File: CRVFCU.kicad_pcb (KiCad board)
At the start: 4 copper layers, 1 part, among them U2 STM32H747IITx

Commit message: completed grouping in pcb, prep for route
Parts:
- added 3V3_PWR1: LED, LED_SMD:LED_0603_1608Metric, F.Cu at (95.3, 149.5)
- added 5V_PWR1: LED, LED_SMD:LED_0603_1608Metric, F.Cu at (96.5, 153.8)
- added ARM1: TERM2.54_01x04, TerminalBlock_TE-Connectivity:TerminalBlock_TE_282834-4_1x04_P2.54mm_Horizontal, F.Cu at (44.0, 102.6)
- added BATT1: AMASS_XT30, Connector_AMASS:AMASS_XT30U-F_1x02_P5.0mm_Vertical, F.Cu at (70.0, 116.0)
- added BZ2: Buzzer, Buzzer_Beeper:Buzzer_CUI_CPT-9019S-SMT, F.Cu at (117.7, 84.6)
- added C1: 100uF, Capacitor_THT:CP_Radial_D8.0mm_P5.00mm, F.Cu at (74.8, 110.4)
- added C10: 1uF, Capacitor_SMD:C_0402_1005Metric, B.Cu at (230.0, 30.9)
- added C11: 4.7uF, Capacitor_SMD:C_0402_1005Metric, B.Cu at (250.9, 49.1)
- added C12: 220pF, Capacitor_SMD:C_0402_1005Metric, B.Cu at (249.6, 50.4)
- added C13: 2.2uF, Capacitor_SMD:C_0402_1005Metric, B.Cu at (239.6, 52.3)
- added C14: 2.2uF, Capacitor_SMD:C_0402_1005Metric, B.Cu at (225.2, 37.7)
- added C15: 2.2uF, Capacitor_SMD:C_0402_1005Metric, B.Cu at (233.9, 26.9)
- added C16: 100nF, Capacitor_SMD:C_0402_1005Metric, B.Cu at (234.6, 27.7)
- added C17: 10uF, Capacitor_SMD:C_0402_1005Metric, B.Cu at (256.8, 39.2)
- added C18: 100nF, Capacitor_SMD:C_0402_1005Metric, B.Cu at (257.6, 40.0)
- added C19: 100nF, Capacitor_SMD:C_0402_1005Metric, B.Cu at (247.8, 47.6)
- added C2: 10uF, Capacitor_SMD:C_0402_1005Metric, F.Cu at (68.5, 108.7)
- added C20: 100nF, Capacitor_SMD:C_0402_1005Metric, B.Cu at (232.4, 28.3)
- added C21: 100nF, Capacitor_SMD:C_0402_1005Metric, B.Cu at (237.0, 23.6)
- added C22: 100nF, Capacitor_SMD:C_0402_1005Metric, B.Cu at (239.6, 21.1)
- added C23: 100nF, Capacitor_SMD:C_0402_1005Metric, B.Cu at (245.5, 21.2)
- added C24: 100nF, Capacitor_SMD:C_0402_1005Metric, B.Cu at (246.9, 22.6)
- added C25: 100nF, Capacitor_SMD:C_0402_1005Metric, B.Cu at (250.2, 25.9)
- added C26: 100nF, Capacitor_SMD:C_0402_1005Metric, B.Cu at (252.4, 28.1)
- added C27: 100nF, Capacitor_SMD:C_0402_1005Metric, B.Cu at (258.5, 34.2)
- added C28: 100nF, Capacitor_SMD:C_0402_1005Metric, B.Cu at (260.2, 37.3)
- added C29: 100nF, Capacitor_SMD:C_0402_1005Metric, B.Cu at (252.3, 45.5)
- added C30: 100nF, Capacitor_SMD:C_0402_1005Metric, B.Cu at (246.1, 51.7)
- added C31: 100nF, Capacitor_SMD:C_0402_1005Metric, B.Cu at (246.4, 48.9)
- added C32: 100nF, Capacitor_SMD:C_0402_1005Metric, B.Cu at (227.4, 33.0)
- added C33: 100nF, Capacitor_SMD:C_0402_1005Metric, B.Cu at (232.1, 45.0)
- added C34: 100nF, Capacitor_SMD:C_0402_1005Metric, B.Cu at (241.2, 53.9)
- added C35: 100nF, Capacitor_SMD:C_0402_1005Metric, B.Cu at (225.4, 40.1)
- added C36: 4.7uF, Capacitor_SMD:C_0402_1005Metric, B.Cu at (226.6, 39.1)
- added C37: 1.5pF, Capacitor_SMD:C_0402_1005Metric, F.Cu at (251.3, 52.5)
- added C38: 1.5pF, Capacitor_SMD:C_0402_1005Metric, F.Cu at (249.9, 53.9)
- added C39: 100nF, Capacitor_SMD:C_0402_1005Metric, B.Cu at (234.9, 47.8)
- added C4: 10uF, Capacitor_SMD:C_0402_1005Metric, F.Cu at (52.4, 94.1)
- added C41: 100nF, Capacitor_SMD:C_0402_1005Metric, F.Cu at (257.0, 42.3)
- added C42: 220nF, Capacitor_SMD:C_0402_1005Metric, B.Cu at (137.0, 164.8)
- added C43: 10uF, Capacitor_SMD:C_0402_1005Metric, B.Cu at (139.0, 163.8)
- added C44: 100nF, Capacitor_SMD:C_0402_1005Metric, B.Cu at (138.9, 162.6)
- added C45: 100nF, Capacitor_SMD:C_0402_1005Metric, B.Cu at (139.0, 164.8)
- added C46: 100nF, Capacitor_SMD:C_0402_1005Metric, B.Cu at (148.1, 162.3)
- added C47: 100nF, Capacitor_SMD:C_0402_1005Metric, B.Cu at (160.1, 164.3)
- added C48: 100nF, Capacitor_SMD:C_0402_1005Metric, B.Cu at (158.2, 164.3)
- added C49: 10nF, Capacitor_SMD:C_0402_1005Metric, F.Cu at (166.3, 163.8)
- added C5: 10uF, Capacitor_SMD:C_0402_1005Metric, F.Cu at (62.3, 89.1)
- added C50: 100nF, Capacitor_SMD:C_0402_1005Metric, F.Cu at (260.5, 46.3)
- added C51: 100nF, Capacitor_SMD:C_0402_1005Metric, B.Cu at (252.3, 41.3)
- added C6: 10uF, Capacitor_SMD:C_0402_1005Metric, F.Cu at (62.3, 91.5)
- added C7: 10uF, Capacitor_SMD:C_0402_1005Metric, F.Cu at (52.3, 104.7)
- added C8: 10uF, Capacitor_SMD:C_0402_1005Metric, F.Cu at (62.3, 100.2)
- added C9: 10uF, Capacitor_SMD:C_0402_1005Metric, F.Cu at (62.3, 102.5)
- added D1: MBR0540, Diode_SMD:D_SOD-123, F.Cu at (59.4, 95.5)
- added D2: MBR0540, Diode_SMD:D_SOD-123, F.Cu at (59.3, 106.5)
- added H1: MountingHole_Pad, MountingHole:MountingHole_3.2mm_M3_Pad, F.Cu at (44.0, 116.0)
- added H2: MountingHole_Pad, MountingHole:MountingHole_3.2mm_M3_Pad, F.Cu at (-23.0, 91.0)
- added H3: MountingHole_Pad, MountingHole:MountingHole_3.2mm_M3_Pad, F.Cu at (-23.0, 99.0)
- added H4: MountingHole_Pad, MountingHole:MountingHole_3.2mm_M3_Pad, F.Cu at (86.0, 116.0)
- added J1: TagConnect_TC2030, Connector:Tag-Connect_TC2030-IDC-NL_2x03_P1.27mm_Vertical, F.Cu at (213.4, 77.3)
- added J3: USB_C_Receptacle_USB2.0_16P, Connector_USB:USB_C_Receptacle_GCT_USB4105-xx-A_16P_TopMnt_Horizontal, F.Cu at (131.9, 65.9)
- added J4: Micro_SD_Card_Det2, Connector_Card:microSD_HC_Hirose_DM3AT-SF-PEJM5, B.Cu at (49.2, 28.4)
- added L1: 1608KF-601T03, Inductor_SMD:L_0603_1608Metric, B.Cu at (256.8, 37.4)
- added L2: FBMJ1608HM180NTR, Inductor_SMD:L_0603_1608Metric, B.Cu at (250.0, 47.2)
- added L3: 2.2uH, Inductor_SMD:L_0603_1608Metric, B.Cu at (247.8, 49.4)
- added LED1: LED, LED_SMD:LED_0603_1608Metric, F.Cu at (110.1, 157.0)
- added NEOPIX1: WS2812B-2020, LED_SMD:LED_WS2812B-2020_PLCC4_2.0x2.0mm, F.Cu at (149.3, 127.7)
- added PWM0: JST_XH_B3B-XH-AM, Connector_PinHeader_2.54mm:PinHeader_1x03_P2.54mm_Vertical, F.Cu at (47.1, 88.0)
- added PWM1: JST_XH_B3B-XH-AM, Connector_PinHeader_2.54mm:PinHeader_1x03_P2.54mm_Vertical, F.Cu at (47.1, 91.6)
- added PWM2: JST_XH_B3B-XH-AM, Connector_PinHeader_2.54mm:PinHeader_1x03_P2.54mm_Vertical, F.Cu at (47.1, 95.2)
- added PWM3: JST_XH_B3B-XH-AM, Connector_PinHeader_2.54mm:PinHeader_1x03_P2.54mm_Vertical, F.Cu at (47.1, 98.8)
- added PWM4: JST_XH_B3B-XH-AM, Connector_PinHeader_2.54mm:PinHeader_1x03_P2.54mm_Vertical, F.Cu at (50.0, 112.9)
- added PWM5: JST_XH_B3B-XH-AM, Connector_PinHeader_2.54mm:PinHeader_1x03_P2.54mm_Vertical, F.Cu at (53.6, 112.9)
- added PWM6: JST_XH_B3B-XH-AM, Connector_PinHeader_2.54mm:PinHeader_1x03_P2.54mm_Vertical, F.Cu at (57.2, 112.9)
- added PWM7: JST_XH_B3B-XH-AM, Connector_PinHeader_2.54mm:PinHeader_1x03_P2.54mm_Vertical, F.Cu at (60.8, 112.9)
- added PYRO_TERM1: TERM2.54_01x10, TerminalBlock_TE-Connectivity:TerminalBlock_TE_1-282834-0_1x10_P2.54mm_Horizontal, F.Cu at (86.0, 109.9)
- added Q3: DMG2301L, Package_TO_SOT_SMD:SOT-23, F.Cu at (54.9, 96.0)
- added Q4: BC818, Package_TO_SOT_SMD:SOT-23, F.Cu at (119.3, 94.5)
- added Q5: DMG2301L, Package_TO_SOT_SMD:SOT-23, F.Cu at (250.2, 71.7)
- added Q6: DMG2301L, Package_TO_SOT_SMD:SOT-23, F.Cu at (54.9, 107.1)
- added R1: 10k, Resistor_SMD:R_Array_Convex_4x0402, F.Cu at (215.0, 74.1)
- added R10: 10k, Resistor_SMD:R_0402_1005Metric, B.Cu at (62.3, 108.2)
- added R11: 3.3k, Resistor_SMD:R_0402_1005Metric, B.Cu at (77.1, 100.5)
- added R12: 1k, Resistor_SMD:R_0402_1005Metric, B.Cu at (77.1, 99.5)
- added R13: 5.1k, Resistor_SMD:R_0402_1005Metric, F.Cu at (137.7, 63.9)
- added R14: 180k, Resistor_SMD:R_0402_1005Metric, B.Cu at (81.1, 98.6)
- added R15: 10k, Resistor_SMD:R_Array_Convex_2x0402, F.Cu at (147.6, 135.4)
- added R16: 56k, Resistor_SMD:R_0402_1005Metric, B.Cu at (79.1, 98.6)
- added R17: 5.1k, Resistor_SMD:R_0402_1005Metric, F.Cu at (137.7, 68.4)
- added R18: 47R, Resistor_SMD:R_0402_1005Metric, F.Cu at (161.2, 163.4)
- added R19: 3.3k, Resistor_SMD:R_0402_1005Metric, B.Cu at (77.1, 102.5)
- added R2: 10k, Resistor_SMD:R_0402_1005Metric, F.Cu at (58.0, 97.2)
- added R20: 10k, Resistor_SMD:R_0402_1005Metric, B.Cu at (158.2, 163.3)
- added R21: 10k, Resistor_SMD:R_0402_1005Metric, B.Cu at (148.1, 164.7)
- added R22: 10k, Resistor_SMD:R_0402_1005Metric, B.Cu at (137.0, 163.8)
- added R23: 10k, Resistor_SMD:R_0402_1005Metric, B.Cu at (248.5, 45.2)
- added R24: 10k, Resistor_SMD:R_0402_1005Metric, B.Cu at (59.3, 34.2)
- added R25: 1k, Resistor_SMD:R_0402_1005Metric, B.Cu at (77.1, 101.5)
- added R26: 180k, Resistor_SMD:R_0402_1005Metric, B.Cu at (81.1, 103.4)
- added R27: 56k, Resistor_SMD:R_0402_1005Metric, B.Cu at (79.1, 103.4)
- added R28: 3.3k, Resistor_SMD:R_0402_1005Metric, B.Cu at (77.1, 90.1)
- added R29: 1k, Resistor_SMD:R_0402_1005Metric, B.Cu at (77.1, 89.1)
- added R30: 180k, Resistor_SMD:R_0402_1005Metric, B.Cu at (81.1, 88.4)
- added R31: 56k, Resistor_SMD:R_0402_1005Metric, B.Cu at (79.1, 88.4)
- added R32: 3.3k, Resistor_SMD:R_0402_1005Metric, B.Cu at (77.1, 92.1)
- added R33: 1k, Resistor_SMD:R_0402_1005Metric, B.Cu at (77.1, 91.1)
- added R34: 180k, Resistor_SMD:R_0402_1005Metric, B.Cu at (81.1, 93.2)
- added R35: 56k, Resistor_SMD:R_0402_1005Metric, B.Cu at (79.1, 93.2)
- added R36: 220R, Resistor_SMD:R_0402_1005Metric, B.Cu at (96.5, 153.8)
- added R37: 220R, Resistor_SMD:R_0402_1005Metric, B.Cu at (95.2, 149.5)
- added R38: 47R, Resistor_SMD:R_Array_Convex_4x0402, B.Cu at (50.1, 94.0)
- added R39: 47R, Resistor_SMD:R_Array_Convex_4x0402, B.Cu at (55.5, 109.9)
- added R4: 47R1%, Resistor_SMD:R_0402_1005Metric, B.Cu at (258.6, 41.1)
- added R40: 10k, Resistor_SMD:R_0402_1005Metric, F.Cu at (125.6, 93.3)
- added R41: 2.2k, Resistor_SMD:R_0402_1005Metric, F.Cu at (125.1, 90.9)
- added R42: 220R, Resistor_SMD:R_0402_1005Metric, F.Cu at (109.8, 159.8)
- added R43: 10k, Resistor_SMD:R_0402_1005Metric, B.Cu at (50.4, 104.0)
- added R44: 47R, Resistor_SMD:R_0402_1005Metric, B.Cu at (50.4, 105.1)
- added R45: 10k, Resistor_SMD:R_0402_1005Metric, F.Cu at (247.6, 71.7)
- added R5: 10k, Resistor_SMD:R_0402_1005Metric, B.Cu at (239.2, 54.0)
- added R6: 10k, Resistor_SMD:R_0402_1005Metric, B.Cu at (237.4, 49.9)
- added R7: 10k, Resistor_SMD:R_0402_1005Metric, F.Cu at (166.3, 162.0)
- added R8: 51, Resistor_SMD:R_0402_1005Metric, F.Cu at (256.3, 43.6)
- added R9: 10k, Resistor_SMD:R_0402_1005Metric, F.Cu at (261.8, 45.0)
- added RADIO_5VPWR_3V3IO1: JST_GH_SM06B, Connector_JST:JST_GH_SM06B-GHS-TB_1x06-1MP_P1.25mm_Horizontal, F.Cu at (229.4, 76.0)
- added STEMMA_QT1: JST_SH_SM04B, Connector_JST:JST_SH_SM04B-SRSS-TB_1x04-1MP_P1.00mm_Horizontal, F.Cu at (120.7, 139.1)
- added SW1: SW_Omron_B3FS, Button_Switch_SMD:SW_SPST_FSMSM, F.Cu at (263.4, 36.3)
- added SW2: SW_Nidec_CAS-120A1, Button_Switch_SMD:Nidec_Copal_CAS-120A, F.Cu at (235.0, 52.4)
- added U1: MS5611-01BA, Package_LGA:LGA-8_3x5mm_P1.25mm, F.Cu at (149.1, 163.5)
- added U10: W25Q128JVS, Package_SO:SOIC-8_5.3x5.3mm_P1.27mm, B.Cu at (247.5, 41.3)
- added U11: CM1624, Package_DFN_QFN:OnSemi_UDFN-16-1EP_1.35x3.3mm_P0.4mm_EP0.4x2.8mm, B.Cu at (59.3, 29.0)
- added U12: ~, Package_TO_SOT_SMD:SOT-353_SC-70-5, F.Cu at (212.1, 73.6)
- added U13: USBLC6-2SC6, Package_TO_SOT_SMD:SOT-23-6, F.Cu at (121.6, 132.5)
- added U14: USBLC6-2SC6, Package_TO_SOT_SMD:SOT-23-6, F.Cu at (138.8, 66.2)
- added U15: MAX17049, Package_DFN_QFN:TDFN-8-1EP_2x2mm_P0.5mm_EP0.8x1.2mm, F.Cu at (144.6, 136.0)
- added U16: SI7232DN-T1, FCU2025Lib:SQJ500AEP-T1_GE3_VIS, B.Cu at (79.9, 90.8)
- added U17: SN74LV1T34DCK, Package_TO_SOT_SMD:SOT-353_SC-70-5, B.Cu at (149.3, 127.6)
- added U3: LIS2MDL, Package_LGA:LGA-12_2x2mm_P0.5mm, F.Cu at (138.3, 163.6)
- added U4: ICM-45686, Package_LGA:LGA-14_3x2.5mm_P0.5mm_LayoutBorder3x4y, F.Cu at (158.8, 163.3)
- added U5: FXMA108, Package_DFN_QFN:WQFN-20-1EP_2.5x4.5mm_P0.5mm_EP1x2.9mm, B.Cu at (59.1, 105.9)
- added U6: AP1117-50, Package_TO_SOT_SMD:SOT-223-3_TabPin2, F.Cu at (57.3, 90.6)
- added U7: AP1117-33, Package_TO_SOT_SMD:SOT-223-3_TabPin2, F.Cu at (57.4, 101.6)
- added U8: SI7232DN-T1, FCU2025Lib:SQJ500AEP-T1_GE3_VIS, B.Cu at (79.9, 101.0)
- added U9: USBLC6-4SC6, Package_TO_SOT_SMD:SOT-23-6, F.Cu at (229.0, 69.9)
- added VIDEO1: JST_GH_SM02B, Connector_JST:JST_GH_SM02B-GHS-TB_1x02-1MP_P1.25mm_Horizontal, F.Cu at (249.9, 77.9)
- added Y1: 32.768khz, Crystal:Crystal_SMD_3215-2Pin_3.2x1.5mm, F.Cu at (249.0, 51.8)
- added Y3: 32.768khz, Oscillator:Oscillator_SMD_Abracon_ASE-4Pin_3.2x2.5mm, F.Cu at (163.7, 163.1)
- added Y4: 25MHZ, Oscillator:Oscillator_SMD_Abracon_ASE-4Pin_3.2x2.5mm, F.Cu at (259.5, 43.6)
- moved U2 206.3 mm to (242.4, 36.8), turned to 135 degrees
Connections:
- U2 pad 1: unconnected-(U2-PE2-Pad1) -> /BUZZ
- U2 pad 10: unconnected-(U2-PC14-Pad10) -> /PC14
- U2 pad 101: unconnected-(U2-VCAPDSI-Pad101) -> /VDD12DSI
- U2 pad 102: +1V2 -> /VDD12DSI
- U2 pad 108: +1V2 -> /VDD12DSI
- U2 pad 11: unconnected-(U2-PC15-Pad11) -> /PC15
- U2 pad 116: unconnected-(U2-PG6-Pad116) -> /FLASH_CS
- U2 pad 120: unconnected-(U2-VDD50_USB-Pad120) -> +3V3
- U2 pad 124: unconnected-(U2-PC8-Pad124) -> /SD_DAT0
- U2 pad 125: unconnected-(U2-PC9-Pad125) -> /SD_DAT1
- U2 pad 130: unconnected-(U2-PA11-Pad130) -> /USB_D-
- U2 pad 131: unconnected-(U2-PA12-Pad131) -> /USB_D+
- U2 pad 132: unconnected-(U2-PA13-Pad132) -> /SWDIO
- U2 pad 133: unconnected-(U2-VCAP-Pad133) -> Net-(C13-Pad1)
- U2 pad 138: unconnected-(U2-PA14-Pad138) -> /SWCLK
- U2 pad 140: unconnected-(U2-PC10-Pad140) -> /SD_DAT2
- U2 pad 141: unconnected-(U2-PC11-Pad141) -> /SD_DAT3
- U2 pad 142: unconnected-(U2-PC12-Pad142) -> /SD_CLK
- U2 pad 143: unconnected-(U2-PD0-Pad143) -> /RAD_RX
- U2 pad 144: unconnected-(U2-PD1-Pad144) -> /RAD_TX
- U2 pad 145: unconnected-(U2-PD2-Pad145) -> /SD_CMD
- U2 pad 146: unconnected-(U2-PD3-Pad146) -> /SD_DET
- U2 pad 147: unconnected-(U2-PD4-Pad147) -> /SRV_OE
- U2 pad 148: unconnected-(U2-PD5-Pad148) -> /SRVI_0
- U2 pad 149: unconnected-(U2-PD6-Pad149) -> /SRVI_1
- U2 pad 15: unconnected-(U2-VLXSMPS-Pad15) -> /VLXSMPS
- U2 pad 150: unconnected-(U2-PD7-Pad150) -> /SRVI_2
- U2 pad 153: unconnected-(U2-PG9-Pad153) -> /SRVI_3
- U2 pad 154: unconnected-(U2-PG10-Pad154) -> /SRVI_4
- U2 pad 155: unconnected-(U2-PG11-Pad155) -> /SRVI_5
- U2 pad 156: unconnected-(U2-PG12-Pad156) -> /SRVI_6
- U2 pad 157: unconnected-(U2-PG13-Pad157) -> /SRVI_7
- U2 pad 16: +3V3 -> /VDDSMPS
- U2 pad 162: unconnected-(U2-PB3-Pad162) -> /SWO
- U2 pad 167: unconnected-(U2-BOOT0-Pad167) -> Net-(U2-BOOT0)
- U2 pad 17: unconnected-(U2-VFBSMPS-Pad17) -> +3V3
- U2 pad 172: unconnected-(U2-VCAP-Pad172) -> Net-(C13-Pad1)
- U2 pad 174: unconnected-(U2-PDR_ON-Pad174) -> Net-(U2-PDR_ON)
- U2 pad 18: unconnected-(U2-PF0-Pad18) -> /VIDEO
- U2 pad 19: unconnected-(U2-PF1-Pad19) -> /ARM
- U2 pad 20: unconnected-(U2-PF2-Pad20) -> /LED
- U2 pad 21: unconnected-(U2-PF3-Pad21) -> /NEOPIX
- U2 pad 26: unconnected-(U2-PF6-Pad26) -> /QSPI_IO3
- U2 pad 27: unconnected-(U2-PF7-Pad27) -> /QSPI_IO2
- U2 pad 28: unconnected-(U2-PF8-Pad28) -> /QSPI_IO0
- U2 pad 29: unconnected-(U2-PF9-Pad29) -> /QSPI_IO1
- U2 pad 30: unconnected-(U2-PF10-Pad30) -> /QSPI_CLK
- U2 pad 31: unconnected-(U2-PH0-Pad31) -> /OSC0
- U2 pad 33: unconnected-(U2-NRST-Pad33) -> /RESET
- U2 pad 39: unconnected-(U2-VREF+-Pad39) -> Net-(U2-VREF+)
- U2 pad 40: +3V3 -> /VDDA
- U2 pad 46: unconnected-(U2-PA3-Pad46) -> /IMU_INT
- U2 pad 50: unconnected-(U2-PA5-Pad50) -> /SCK
- U2 pad 51: unconnected-(U2-PA6-Pad51) -> /MISO
- U2 pad 52: unconnected-(U2-PA7-Pad52) -> /MOSI
- U2 pad 53: unconnected-(U2-PC4-Pad53) -> /ALT_CS
- U2 pad 54: unconnected-(U2-PC5-Pad54) -> /IMU_CS
- U2 pad 55: unconnected-(U2-PB0-Pad55) -> /MAG_CS
- U2 pad 67: unconnected-(U2-PE7-Pad67) -> /PYR0
- U2 pad 68: unconnected-(U2-PE8-Pad68) -> /PYC0
- U2 pad 69: unconnected-(U2-PE9-Pad69) -> /PYR1
- U2 pad 72: unconnected-(U2-PE10-Pad72) -> /PYC1
- U2 pad 73: unconnected-(U2-PE11-Pad73) -> /PYR2
- U2 pad 74: unconnected-(U2-PE12-Pad74) -> /PYC2
- U2 pad 75: unconnected-(U2-PE13-Pad75) -> /PYR3
- U2 pad 76: unconnected-(U2-PE14-Pad76) -> /PYC3
- U2 pad 78: unconnected-(U2-PB10-Pad78) -> /SCL
- U2 pad 79: unconnected-(U2-PB11-Pad79) -> /SDA
- U2 pad 80: unconnected-(U2-VCAP-Pad80) -> Net-(C13-Pad1)
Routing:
- net +3V3: track 0.00 -> 76.1 mm, vias 0 -> 38
- net unconnected-(J4-SHIELD-Pad11): track 0.00 -> 42.3 mm
- net GND: track 0.00 -> 41.9 mm, vias 0 -> 28
- net VBUS: track 0.00 -> 41.0 mm
- net /FLASH_CS: track 0.00 -> 25.7 mm, vias 0 -> 1
- net +8V4: track 0.00 -> 23.7 mm
- net Net-(J4-DET_A): track 0.00 -> 23.6 mm
- net Net-(U5-B3): track 0.00 -> 14.9 mm
- net Net-(U5-B2): track 0.00 -> 14.8 mm
- net Net-(U5-B1): track 0.00 -> 14.7 mm
- net Net-(U5-B0): track 0.00 -> 14.7 mm
- net +5V: track 0.00 -> 13.8 mm, vias 0 -> 2
- net /SWDIO: track 0.00 -> 10.6 mm
- net /QSPI_IO2: track 0.00 -> 10.0 mm, vias 0 -> 1
- net /QSPI_IO1: track 0.00 -> 9.42 mm, vias 0 -> 1
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- added copper zone on F.Cu, net +3V3
- added copper zone on In2.Cu, net +3V3
- added copper zone on F.Cu, net +5V
- added copper zone on B.Cu, net +8V4
- added copper zone on B.Cu, net /PYO0
- added copper zone on B.Cu, net /PYO1
- added copper zone on B.Cu, net /PYO2
- added copper zone on B.Cu, net /PYO3
- added copper zone on F.Cu, net /VPYRO
- added copper zone on B.Cu, net GND
- added copper zone on F.Cu, net GND
- added copper zone on In1.Cu, net GND
- added copper zone on F.Cu, net Net-(D2-K)
- added copper zone on F.Cu, net Net-(Q3-S)
- added copper zone on F.Cu, net VBAT
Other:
- board outline added: 50 x 100 mm

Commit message: completed 50x100 routing, attempting 40mm
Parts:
- added C40: 100nF, Capacitor_SMD:C_0402_1005Metric, B.Cu at (44.5, 64.7)
- R42: moved to B.Cu
- moved VIDEO1 206.9 mm to (43.2, 69.4), turned to -90 degrees
- moved Q5 200.8 mm to (49.4, 69.7), turned to -90 degrees
- moved C23 198.3 mm to (49.4, 51.0), turned to 45 degrees
- moved R45 198.3 mm to (49.4, 67.2), turned to 180 degrees
- moved C24 197.9 mm to (50.8, 49.6), turned to 45 degrees
- moved C25 197.1 mm to (54.2, 46.3), turned to 45 degrees
- moved C26 196.7 mm to (56.3, 44.1), turned to 45 degrees
- moved C27 196.1 mm to (62.4, 38.0), turned to 45 degrees
- moved C28 194.7 mm to (65.5, 36.4), turned to 135 degrees
- moved C22 193.6 mm to (49.3, 57.0), turned to -45 degrees
- moved L1 191.2 mm to (65.6, 39.7), turned to -45 degrees
- moved C18 189.4 mm to (68.2, 38.9), turned to -45 degrees
- moved C17 189.4 mm to (67.4, 39.7), turned to -45 degrees
- moved R4 189.4 mm to (69.3, 37.9), turned to -45 degrees
- moved R9 188.9 mm to (73.2, 34.7), turned to -45 degrees
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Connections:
- C14 pad 1: Net-(C13-Pad1) -> Net-(C14-Pad1)
- U2 pad 1: /BUZZ -> unconnected-(U2-PE2-Pad1)
- U2 pad 110: unconnected-(U2-PG2-Pad110) -> /ARM
- U2 pad 111: unconnected-(U2-PG3-Pad111) -> /VIDEO
- U2 pad 114: unconnected-(U2-PG4-Pad114) -> /SRVI_7
- U2 pad 115: unconnected-(U2-PG5-Pad115) -> /SRVI_6
- U2 pad 117: unconnected-(U2-PG7-Pad117) -> /SRVI_5
- U2 pad 118: unconnected-(U2-PG8-Pad118) -> /SRVI_4
- U2 pad 122: unconnected-(U2-PC6-Pad122) -> /SRVI_3
- U2 pad 123: unconnected-(U2-PC7-Pad123) -> /SRVI_2
- U2 pad 127: unconnected-(U2-PA8-Pad127) -> /SRVI_1
- U2 pad 128: unconnected-(U2-PA9-Pad128) -> /SRVI_0
- U2 pad 129: unconnected-(U2-PA10-Pad129) -> /SRV_OE
- U2 pad 133: Net-(C13-Pad1) -> Net-(C14-Pad1)
- U2 pad 143: /RAD_RX -> unconnected-(U2-PD0-Pad143)
- U2 pad 144: /RAD_TX -> unconnected-(U2-PD1-Pad144)
- U2 pad 147: /SRV_OE -> unconnected-(U2-PD4-Pad147)
- U2 pad 148: /SRVI_0 -> /BUZZ
- U2 pad 149: /SRVI_1 -> /PYC0
- U2 pad 150: /SRVI_2 -> /PYR0
- U2 pad 153: /SRVI_3 -> unconnected-(U2-PG9-Pad153)
- U2 pad 154: /SRVI_4 -> /PYR1
- U2 pad 155: /SRVI_5 -> /PYC1
- U2 pad 156: /SRVI_6 -> /PYC2
- U2 pad 157: /SRVI_7 -> /PYR2
- U2 pad 158: unconnected-(U2-PG14-Pad158) -> /PYR3
- U2 pad 161: unconnected-(U2-PG15-Pad161) -> /PYC3
- U2 pad 18: /VIDEO -> unconnected-(U2-PF0-Pad18)
- U2 pad 19: /ARM -> unconnected-(U2-PF1-Pad19)
- U2 pad 41: unconnected-(U2-PA0-Pad41) -> /RAD_TX
- U2 pad 42: unconnected-(U2-PA1-Pad42) -> /RAD_RX
- U2 pad 43: unconnected-(U2-PA2-Pad43) -> /RAD_CTS
- U2 pad 46: /IMU_INT -> /RAD_RTS
- U2 pad 49: unconnected-(U2-PA4-Pad49) -> /IMU_INT
- U2 pad 67: /PYR0 -> unconnected-(U2-PE7-Pad67)
- U2 pad 68: /PYC0 -> unconnected-(U2-PE8-Pad68)
- U2 pad 69: /PYR1 -> unconnected-(U2-PE9-Pad69)
- U2 pad 72: /PYC1 -> unconnected-(U2-PE10-Pad72)
- U2 pad 73: /PYR2 -> unconnected-(U2-PE11-Pad73)
- U2 pad 74: /PYC2 -> unconnected-(U2-PE12-Pad74)
- U2 pad 75: /PYR3 -> unconnected-(U2-PE13-Pad75)
- U2 pad 76: /PYC3 -> unconnected-(U2-PE14-Pad76)
- U2 pad 80: Net-(C13-Pad1) -> unconnected-(U2-VCAP-Pad80)
- U2 pad 89: unconnected-(U2-PD8-Pad89) -> /ALRT
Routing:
- net +5V: track 13.8 -> 136.5 mm, vias 2 -> 4
- net /RESET: track 9.32 -> 100.0 mm
- net /SRVI_7: track 0.00 -> 49.2 mm, vias 0 -> 1
- net /SRVI_6: track 0.00 -> 49.0 mm, vias 0 -> 1
- net /SRVI_5: track 0.00 -> 48.5 mm, vias 0 -> 1
- net /SRVI_4: track 0.00 -> 48.5 mm, vias 0 -> 1
- net /SRVI_3: track 0.00 -> 47.6 mm, vias 0 -> 1
- net /SRVI_2: track 0.00 -> 47.6 mm, vias 0 -> 1
- net /SRVI_0: track 0.00 -> 46.7 mm, vias 0 -> 1
- net /SRVI_1: track 0.00 -> 46.5 mm, vias 0 -> 1
- net /SRV_OE: track 3.64 -> 49.2 mm, vias 0 -> 1
- net /PYC0: track 0.98 -> 45.5 mm, vias 0 -> 1
- net /ARM: track 1.10 -> 44.8 mm, vias 0 -> 1
- net /PYC1: track 0.98 -> 40.4 mm, vias 0 -> 1
- net /PYR0: track 1.00 -> 40.3 mm, vias 0 -> 1
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- added copper zone on F.Cu, net +8V4
- added copper zone on F.Cu, net Net-(Q5-S)
- added copper zone on F.Cu, net VBUS
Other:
- board text added: "3V3"
- board text added: "5V"

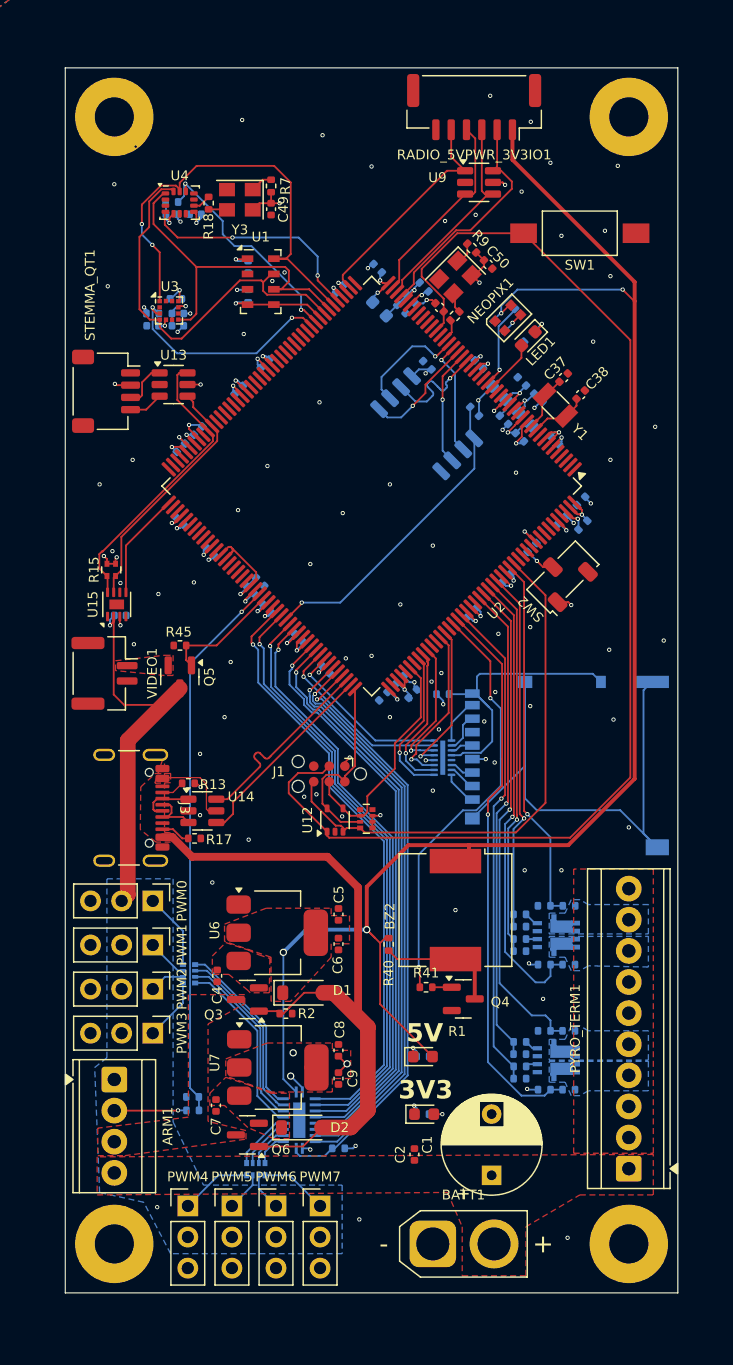
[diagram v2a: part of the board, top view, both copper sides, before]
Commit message: added bom and changed 25mhz oscillator
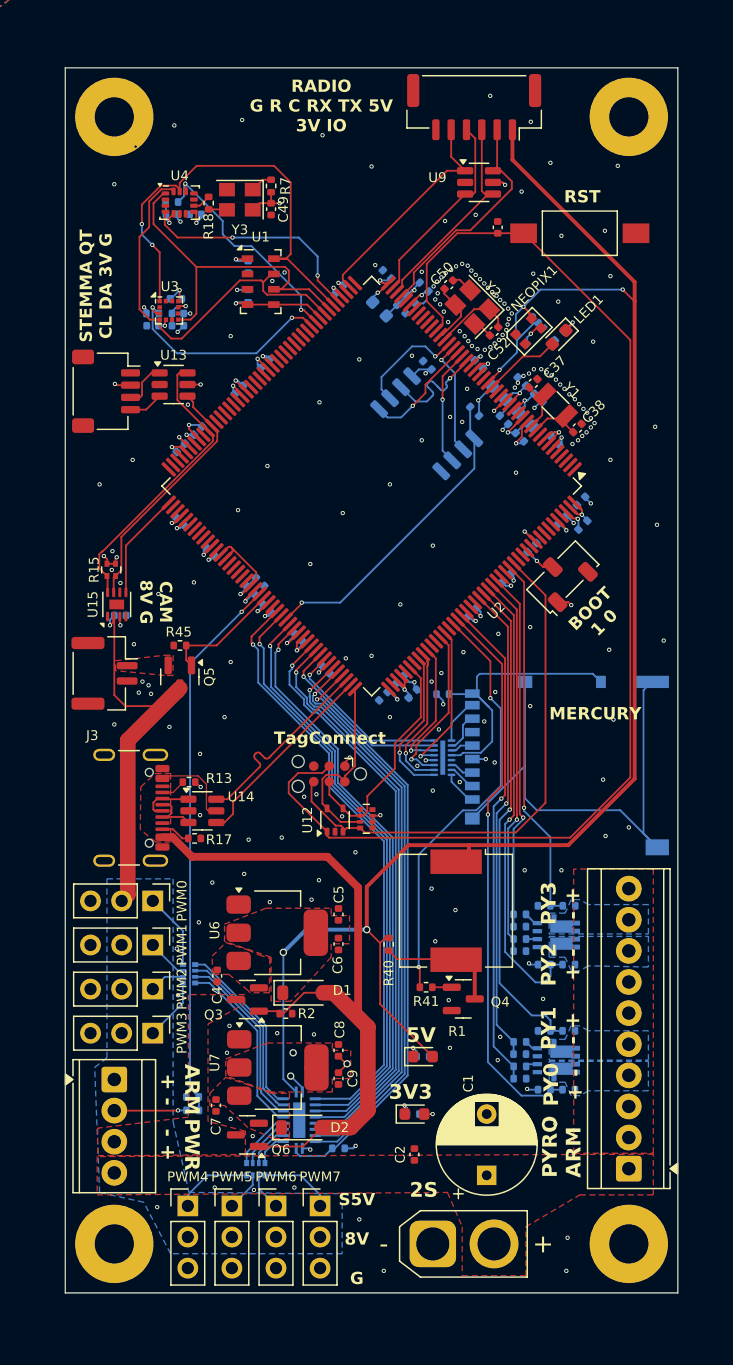
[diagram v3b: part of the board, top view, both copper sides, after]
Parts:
- removed BZ2: Buzzer, Buzzer_Beeper:Buzzer_CUI_CPT-9019S-SMT
- removed R8: 51, Resistor_SMD:R_0402_1005Metric
- removed R9: 10k, Resistor_SMD:R_0402_1005Metric
- removed Y4: 25MHZ, Oscillator:Oscillator_SMD_Abracon_ASE-4Pin_3.2x2.5mm
- added BZ1: Buzzer, Buzzer_Beeper:Buzzer_CUI_CPT-9019S-SMT, F.Cu at (71.9, 88.8)
- added C52: 3.9pF, Capacitor_SMD:C_0402_1005Metric, F.Cu at (75.0, 41.5)
- added Y2: Crystal_GND24, Crystal:Crystal_SMD_3225-4Pin_3.2x2.5mm, F.Cu at (73.2, 39.5)
- C50: value 100nF -> 3.9pF
- R36, R37, R42: value 220R -> 470R
- U12: value ~ -> ESDALC6V1W5
- U16, U8: footprint FCU2025Lib:SQJ500AEP-T1_GE3_VIS -> FCU2025Lib:PowerPak1212-8-Dual
- moved C41 8.07 mm to (75.3, 33.0), turned to -90 degrees
- moved C50 3.61 mm to (71.3, 37.7), turned to 45 degrees
- moved C38 2.74 mm to (81.8, 49.4)
- moved C37 2.52 mm to (78.2, 45.8)
- moved LED1 2.52 mm to (80.3, 42.0)
- moved R42 2.52 mm to (80.3, 41.9)
- moved U17 2.13 mm to (77.9, 41.5)
- moved NEOPIX1 2.00 mm to (77.8, 41.5)
- moved C28 0.92 mm to (66.3, 36.9)
- moved 3V3_PWR1 0.79 mm to (68.5, 105.4)
- moved R37 0.79 mm to (68.4, 105.4)
- moved C1 0.40 mm to (74.4, 110.4)
- moved R13 0.11 mm to (50.1, 78.3)
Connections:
- C50 pad 1: +3V3 -> /OSC1
- U2 pad 32: unconnected-(U2-PH1-Pad32) -> /OSC1
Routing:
- net /OSC1: track 0.00 -> 5.20 mm
- net /OSC0: track 1.69 -> 6.46 mm
- net +3V3: track 90.5 -> 87.2 mm, vias 49 -> 47
- net GND: track 43.0 -> 45.0 mm, vias 99 -> 210
- net /LED: track 4.38 -> 6.35 mm
- net +5V: track 136.5 -> 134.5 mm
- net Net-(Y4-EN): track 1.82 -> 0.00 mm
- net Net-(Y4-OUT): track 1.64 -> 0.00 mm
- net /SRVO_7: track 5.54 -> 6.06 mm
- net /SRVO_4: track 5.84 -> 6.36 mm
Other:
- board text added: "2S"
- board text added: "ARM + -"
- board text added: "BOOT 1 0"
- board text added: "CAM 8V G"
- board text added: "MERCURY"
- board text added: "Mercury H747 FCU V1.0 2025 Kaiwen Zheng"
- board text added: "PWR - +"
- board text added: "PY0 + -"
- board text added: "PY1 - +"
- board text added: "PY2 + -"
- board text added: "PY3 - +"
- board text added: "PYRO ARM"
- board text added: "RADIO G R C RX TX 5V 3V IO"
- board text added: "RST"
- board text added: "S5V 8V G"
- board text added: "STEMMA QT CL DA 3V G"
- board text added: "TagConnect"

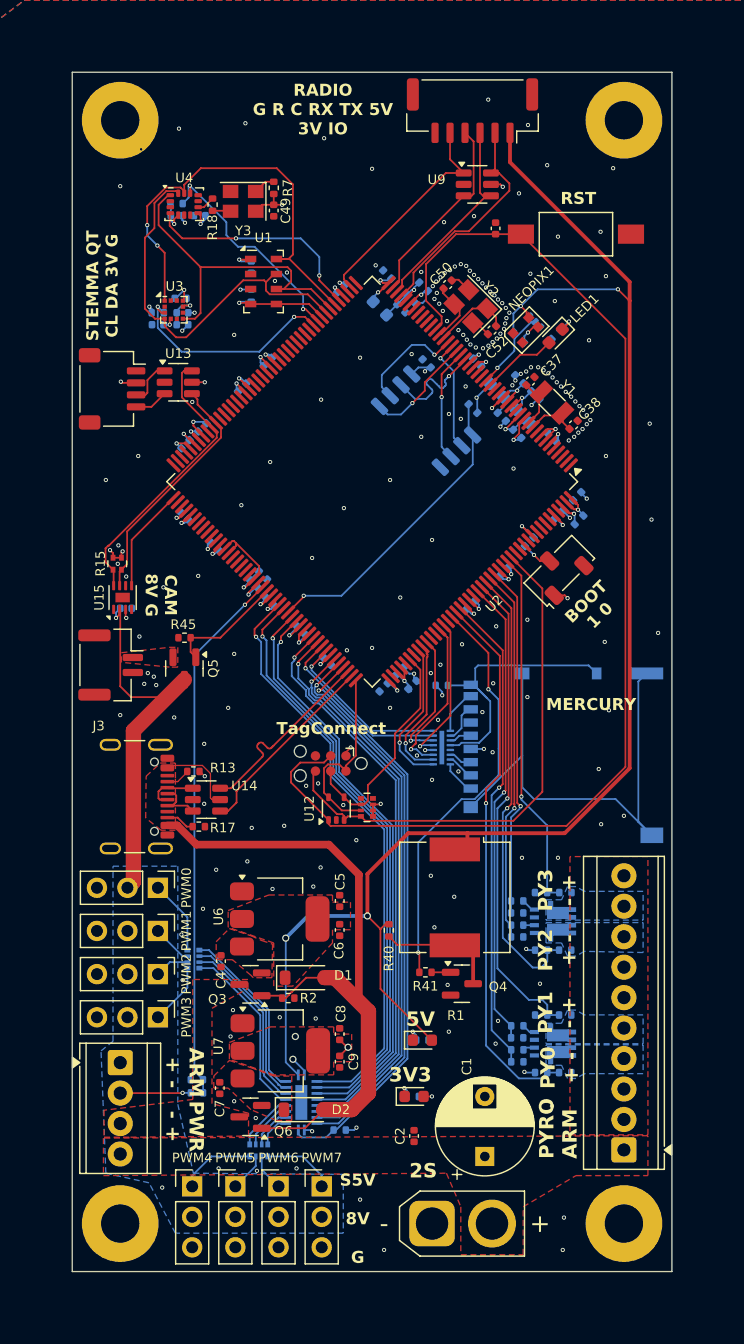
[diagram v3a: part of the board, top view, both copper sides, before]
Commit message: rounded corners, added silkscreens, fixed 25mhz oscillator, missing logos but basically finalized
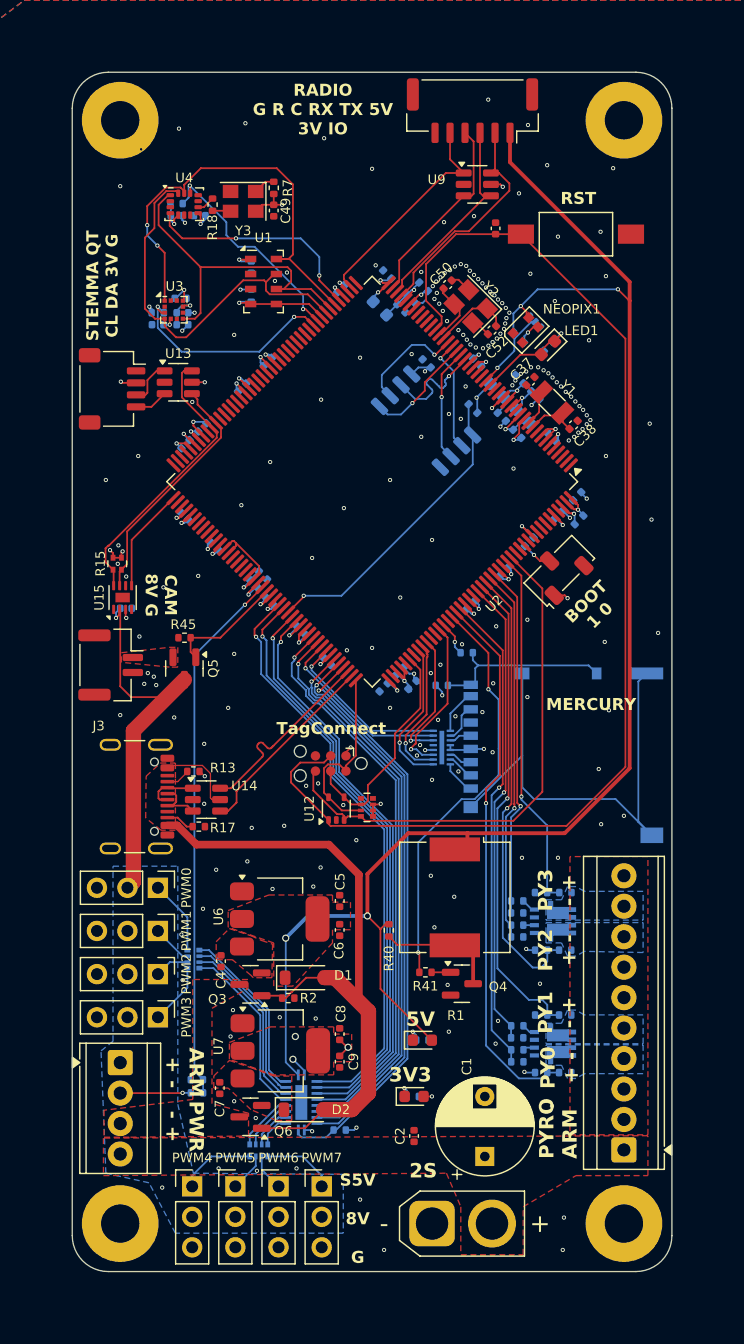
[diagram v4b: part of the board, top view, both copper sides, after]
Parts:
- added R46: 47R, Resistor_SMD:R_0402_1005Metric, B.Cu at (72.9, 68.4)
- U11: value CM1624 -> EClamp2515K
- moved LED1 1.18 mm to (79.7, 43.0)
- moved R42 1.18 mm to (79.7, 42.9)
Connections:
- U11 pad 13: /SD_DET -> unconnected-(U11-ESD1-Pad13)
- U11 pad 4: Net-(J4-DET_A) -> +3V3
- U11 pad 5: unconnected-(U11-ESD3-Pad5) -> +3V3
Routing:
- net /SD_DET: track 12.5 -> 2.88 mm
- net Net-(J4-DET_A): track 23.8 -> 15.4 mm
- net +3V3: track 87.2 -> 89.3 mm
- net GND: vias 210 -> 212
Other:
- outline, holes or cut-outs redrawn
